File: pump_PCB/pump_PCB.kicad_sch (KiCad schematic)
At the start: 0 parts

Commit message: all boards routed: light rev B (SOT-23 switches, protected input), pump rev B (CSD18540 MOSFETs), power rev A1 (parts selected), brain Micro-Fit connectors + display on edge; whitelist gitignore
Light, power and pump pass DRC and ERC clean. Brain routed with 0 unconnected; remaining warnings are dangling vias, thin silk text and missing no-connect flags. All cable connectors standardized to Molex Micro-Fit 3.0. Repo now tracks only the KiCad project files, design rules, local libraries and brain 3D models.
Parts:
- added C1, C2, C3, C4, C5: 0.1uF, Capacitor_THT:C_Disc_D3.8mm_W2.6mm_P2.50mm, symbol Device:C
- added C10, C6, C7, C8, C9: 1uF 25V, Capacitor_THT:C_Disc_D3.8mm_W2.6mm_P2.50mm, symbol Device:C
- added C11: 100uF 25V, Capacitor_THT:CP_Radial_D6.3mm_P2.50mm, symbol Device:C_Polarized
- added D1, D2, D3, D4, D5: 1N4001, Diode_THT:D_DO-41_SOD81_P10.16mm_Horizontal, symbol Device:D
- added J1: CONTROL INPUT, Connector_Molex:Molex_Micro-Fit_3.0_43650-0624_1x06-1MP_P3.00mm_Vertical, symbol Connector_Generic:Conn_01x06
- added J2: POWER INPUT, Connector_Molex:Molex_Micro-Fit_3.0_43650-0324_1x03-1MP_P3.00mm_Vertical, symbol Connector_Generic:Conn_01x03
- added J3: FLORA_GROW, Connector_Molex:Molex_Micro-Fit_3.0_43650-0224_1x02-1MP_P3.00mm_Vertical, symbol Connector_Generic:Conn_01x02
- added J4: FLORA_BLOOM, Connector_Molex:Molex_Micro-Fit_3.0_43650-0224_1x02-1MP_P3.00mm_Vertical, symbol Connector_Generic:Conn_01x02
- added J5: FLORA_MICRO, Connector_Molex:Molex_Micro-Fit_3.0_43650-0224_1x02-1MP_P3.00mm_Vertical, symbol Connector_Generic:Conn_01x02
- added J6: PH_UP, Connector_Molex:Molex_Micro-Fit_3.0_43650-0224_1x02-1MP_P3.00mm_Vertical, symbol Connector_Generic:Conn_01x02
- added J7: PH_DOWN, Connector_Molex:Molex_Micro-Fit_3.0_43650-0224_1x02-1MP_P3.00mm_Vertical, symbol Connector_Generic:Conn_01x02
- added M1, M2, M3, M4, M5: CSD18540Q5B, PumpPower:CSD18540Q5B_TI, symbol PumpPower:CSD18540Q5B
- added R12, R18, R19, R4, R8: 100, Resistor_THT:R_Axial_DIN0207_L6.3mm_D2.5mm_P10.16mm_Horizontal, symbol Device:R
- added R13, R14, R15, R16, R17, R20, R21, R22, R23, R24: 10k, Resistor_THT:R_Axial_DIN0207_L6.3mm_D2.5mm_P10.16mm_Horizontal, symbol Device:R
- added U1, U2, U3, U4, U5: TC4420CPA, Package_DIP:DIP-8_W7.62mm, symbol PumpDrivers:TC4420CPA
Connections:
- new net: R4.1, U1.6 (OUT), U1.7 (OUT)
- new net: M1.4 (G), R15.1, R4.2
- new net: M5.4 (G), R14.1, R19.2
- new net: R8.1, U2.6 (OUT), U2.7 (OUT)
- new net: M2.4 (G), R16.1, R8.2
- new net: R18.1, U4.6 (OUT), U4.7 (OUT)
- new net: M4.4 (G), R13.1, R18.2
- new net: R19.1, U5.6 (OUT), U5.7 (OUT)
- new net: M3.4 (G), R12.2, R17.1
- new net: R12.1, U3.6 (OUT), U3.7 (OUT)
- new net +12V: C1.1, C10.1, C11.1, C2.1, C3.1, C4.1, C5.1, C6.1, C7.1, C8.1, C9.1, D1.1 (K), D2.1 (K), D3.1 (K), D4.1 (K), D5.1 (K), J2.1 (Pin_1), J3.2 (Pin_2), J4.2 (Pin_2), J5.2 (Pin_2), J6.2 (Pin_2), J7.2 (Pin_2), U1.1 (VDD), U1.8 (VDD), U2.1 (VDD), U2.8 (VDD), U3.1 (VDD), U3.8 (VDD), U4.1 (VDD), U4.8 (VDD), U5.1 (VDD), U5.8 (VDD)
- new net +5V: J2.2 (Pin_2)
- new net FLORA_BLOOM: J1.6 (Pin_6), R22.1, U3.2 (IN)
- new net FLORA_BLOOM_SW: D3.2 (A), J4.1 (Pin_1), M3.5 (D)
- new net FLORA_GROW: J1.5 (Pin_5), R21.1, U2.2 (IN)
- new net FLORA_GROW_SW: D2.2 (A), J3.1 (Pin_1), M2.5 (D)
- new net FLORA_MICRO: J1.4 (Pin_4), R20.1, U1.2 (IN)
- new net FLORA_MICRO_SW: D1.2 (A), J5.1 (Pin_1), M1.5 (D)
- new net GND: C1.2, C10.2, C11.2, C2.2, C3.2, C4.2, C5.2, C6.2, C7.2, C8.2, C9.2, J1.1 (Pin_1), J2.3 (Pin_3), M1.1 (S), M1.2 (S), M1.3 (S), M2.1 (S), M2.2 (S), M2.3 (S), M3.1 (S), M3.2 (S), M3.3 (S), M4.1 (S), M4.2 (S), M4.3 (S), M5.1 (S), M5.2 (S), M5.3 (S), R13.2, R14.2, R15.2, R16.2, R17.2, R20.2, R21.2, R22.2, R23.2, R24.2, U1.4 (GND), U1.5 (GND), U2.4 (GND), U2.5 (GND), U3.4 (GND), U3.5 (GND), U4.4 (GND), U4.5 (GND), U5.4 (GND), U5.5 (GND)
- new net PH_DOWN: J1.3 (Pin_3), R24.1, U5.2 (IN)
- new net PH_DOWN_SW: D5.2 (A), J7.1 (Pin_1), M5.5 (D)
- new net PH_UP: J1.2 (Pin_2), R23.1, U4.2 (IN)
- new net PH_UP_SW: D4.2 (A), J6.1 (Pin_1), M4.5 (D)
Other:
- note added: "FLORA_BLOOM (HIGH = ON)"
- note added: "FLORA_GROW (HIGH = ON)"
- note added: "FLORA_MICRO (HIGH = ON)"
- note added: "INTERFACE / POWER"
- note added: "PH_DOWN (HIGH = ON)"
- note added: "PH_UP (HIGH = ON)"
- title: (none) -> Hydroponics - five-channel pump driver

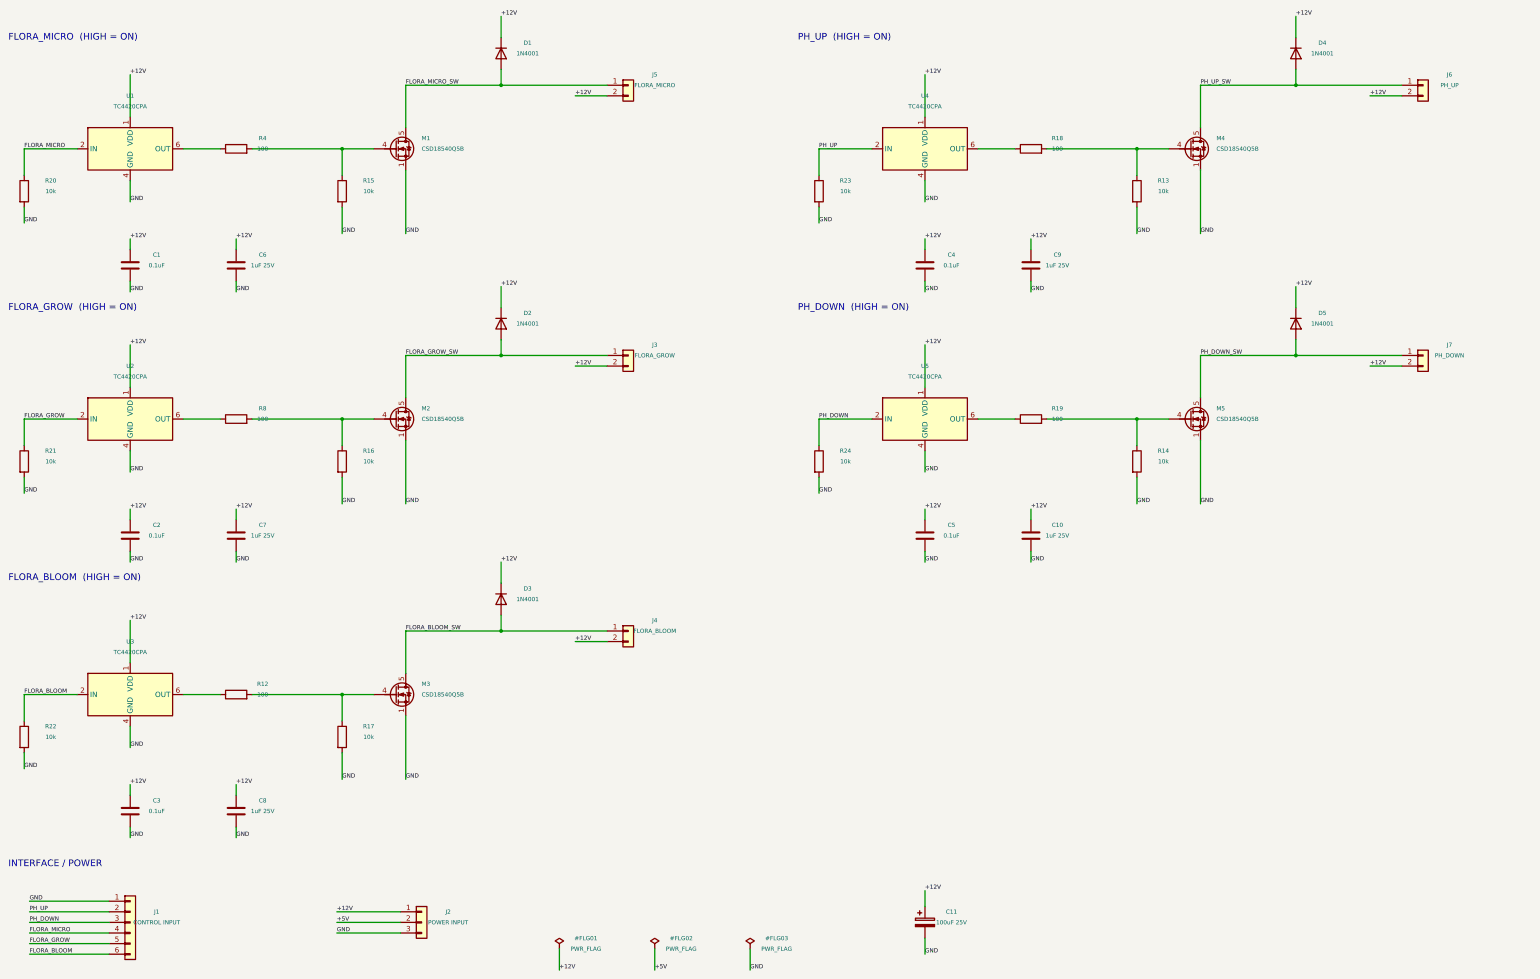
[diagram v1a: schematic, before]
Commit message: Update four KiCad designs and include portable project libraries
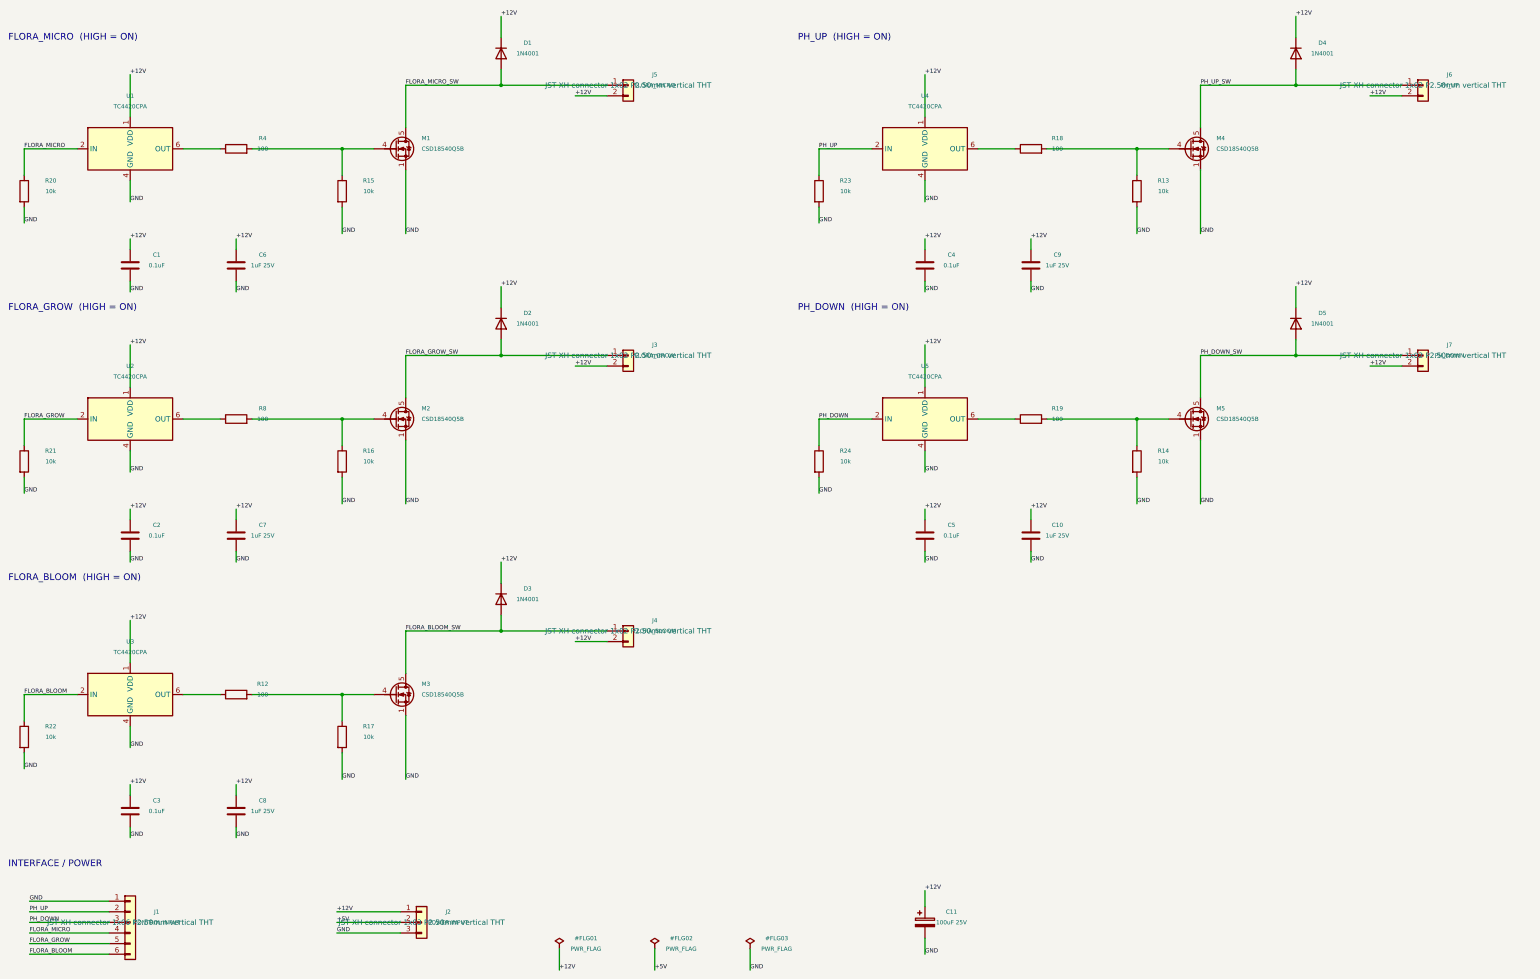
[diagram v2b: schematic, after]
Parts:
- C1, C2, C3, C4, C5: footprint Capacitor_THT:C_Disc_D3.8mm_W2.6mm_P2.50mm -> Capacitor_SMD:C_0603_1608Metric; JLCPCB URL (none) -> https://jlcpcb.com/partdetail/MurataElectronics-GRM188R71H1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; LCSC (none) -> C77055; MPN (none) -> GRM188R71H104KA93D; Manufacturer (none) -> Murata; Rating (none) -> 100nF 50V X7R
- C10, C6, C7, C8, C9: footprint Capacitor_THT:C_Disc_D3.8mm_W2.6mm_P2.50mm -> Capacitor_SMD:C_0603_1608Metric; JLCPCB URL (none) -> https://jlcpcb.com/partdetail/MurataElectronics-GRM188R71E1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; LCSC (none) -> C86020; MPN (none) -> GRM188R71E105KA12D; Manufacturer (none) -> Murata; Rating (none) -> 1uF 25V X7R
- C11: JLCPCB URL (none) -> https://jlcpcb.com/partdetail/PANASONIC-EEUFM1E101/C713389; LCSC (none) -> C713389; MPN (none) -> EEUFM1E101; Manufacturer (none) -> PANASONIC; Rating (none) -> 100uF 25V, 6.3mm diameter x 11.2mm height, 2.5mm pitch; Release Status (none) -> Stocked discontinued FM part accepted for small build; 2000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; Replacement Review (none) -> Panasonic FM 100uF 25V, diameter 6.3mm, height 11.2mm, 2.5m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; Sourcing Status (none) -> Catalog checked for 3 boards of each design; stock not rese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
- D1, D2, D3, D4, D5: JLCPCB URL (none) -> https://jlcpcb.com/partdetail/VishayIntertech-1N4001_E354/C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; LCSC (none) -> C145305; MPN (none) -> 1N4001-E3/54; Manufacturer (none) -> Vishay; Rating (none) -> 1A, 50V, DO-41; Release Status (none) -> HOLD: actual motor current/turn-off energy; on/off drive on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
- J1: footprint Connector_Molex:Molex_Micro-Fit_3.0_43650-0624_1x06-1MP_P3.00mm_Vertical -> Connector_JST:JST_XH_B6B-XH-A_1x06_P2.50mm_Vertical; MPN 436500624 -> B6B-XH-A(LF)(SN); Manufacturer Molex -> JST (XH-compatible clone OK); Replacement Review (none) -> JST XH 2.50mm vertical THT, hand-soldered (Taiss XH kit, Am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; Selection Notes (none) -> JST XH 2.50mm vertical THT, hand-soldered (Taiss XH kit, Am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; Sourcing Status (none) -> JST XH 2.50mm vertical THT, hand-soldered (Taiss XH kit, Am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
- J2: footprint Connector_Molex:Molex_Micro-Fit_3.0_43650-0324_1x03-1MP_P3.00mm_Vertical -> Connector_JST:JST_XH_B3B-XH-A_1x03_P2.50mm_Vertical; Cable Contact (none) -> SXH-001T-P0.6; MPN 436500324 -> B3B-XH-A(LF)(SN); Manufacturer Molex -> JST (XH-compatible clone OK); Mating Housing (none) -> XHP-3; Replacement Review (none) -> JST XH 2.50mm vertical THT, hand-soldered (Taiss XH kit, Am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; Selection Notes (none) -> JST XH 2.50mm vertical THT, hand-soldered (Taiss XH kit, Am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; Sourcing Status (none) -> JST XH 2.50mm vertical THT, hand-soldered (Taiss XH kit, Am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
- J3, J4, J5, J6, J7: footprint Connector_Molex:Molex_Micro-Fit_3.0_43650-0224_1x02-1MP_P3.00mm_Vertical -> Connector_JST:JST_XH_B2B-XH-A_1x02_P2.50mm_Vertical; MPN 436500224 -> B2B-XH-A(LF)(SN); Manufacturer Molex -> JST (XH-compatible clone OK)
- M1, M2, M3, M4, M5: JLCPCB URL (none) -> https://jlcpcb.com/partdetail/TexasInstruments-CSD18540Q5B/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; LCSC (none) -> C86513
- R12, R18, R19, R4, R8: JLCPCB URL (none) -> https://jlcpcb.com/partdetail/YAGEO-MFR_25FBF52100R/C6300650; LCSC (none) -> C6300650; MPN (none) -> MFR-25FBF52-100R; Manufacturer (none) -> Yageo; Rating (none) -> 1%, 0.25W axial; formed 10.16mm lead pitch
- R13, R14, R15, R16, R17, R20, R21, R22, R23, R24: JLCPCB URL (none) -> https://jlcpcb.com/partdetail/YAGEO-MFR_25FBF5210K/C1519255; LCSC (none) -> C1519255; MPN (none) -> MFR-25FBF52-10K; Manufacturer (none) -> Yageo; Rating (none) -> 1%, 0.25W axial; formed 10.16mm lead pitch
- U1, U2, U3, U4, U5: JLCPCB URL (none) -> https://jlcpcb.com/partdetail/MicrochipTech-TC4420CPA/C48733; LCSC (none) -> C48733; MPN (none) -> TC4420CPA; Manufacturer (none) -> Microchip; Rating (none) -> Non-inverting driver, PDIP8; 12V gate rail
